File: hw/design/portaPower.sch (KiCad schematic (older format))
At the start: 5 parts

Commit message: aux output, documentation
finished aux output circuit, updated a lot of documentation, added datasheets
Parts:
- removed A?: Arduino_Nano_v3.x, Module:Arduino_Nano, symbol MCU_Module:Arduino_Nano_v3.x
- added H?: EARTH, MountingHole:MountingHole_4.3mm_M4_Pad, symbol Mechanical:MountingHole_Pad
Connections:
- net labels added: Earth_Protective, L, L_filt, N, N_filt
- wire segments 55 -> 47
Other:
- note added: "All resistors 0603 size unless otherwise stated\nAll capacitors 0603 size unless otherwise stated\nAll capacitors rated for 16V unless otherwise stated"
- note added: "Auxiliary\n5V Output"
- note added: "M4 thru hole"
- note added: "System\nRegulator"
- note removed: "Auxiliary Output &\nSecondary Regulators"
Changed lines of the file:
@@
 $Descr A4 11693 8268
 encoding utf-8
-Sheet 1 6
+Sheet 1 7
 Title ""
 Date ""
@@
 F14 "~ALT_2A" B L 5500 3550 50
 $EndSheet
-Text Notes 1350 1650 0    50   ~ 0
+Text Notes 1300 1200 0    50   ~ 0
 Line AC
 Wire Wire Line
@@
 Wire Wire Line
 	6500 3550 7600 3550
-Wire Wire Line
-	7600 3550 7600 2900
 Wire Wire Line
 	7600 1850 7950 1850
@@
 L power:GND #PWR?
 U 1 1 5EC49D4C
-P 2700 4600
-F 0 "#PWR?" H 2700 4350 50  0001 C CNN
-F 1 "GND" H 2705 4427 50  0000 C CNN
-F 2 "" H 2700 4600 50  0001 C CNN
-F 3 "" H 2700 4600 50  0001 C CNN
-	1    2700 4600
-	1    0    0    -1
-$EndComp
-Wire Wire Line
-	2700 4600 2700 4400
-Wire Wire Line
-	2700 4400 2600 4400
-Text Notes 1400 3200 0    100  ~ 0
-Auxiliary Output &\nSecondary Regulators
-$Sheet
-S 1700 3750 900  800
+P 2600 6700
+F 0 "#PWR?" H 2600 6450 50  0001 C CNN
+F 1 "GND" H 2605 6527 50  0000 C CNN
+F 2 "" H 2600 6700 50  0001 C CNN
+F 3 "" H 2600 6700 50  0001 C CNN
+	1    2600 6700
+	1    0    0    -1
+$EndComp
+Wire Wire Line
+	2600 6700 2600 6500
+Wire Wire Line
+	2600 6500 2500 6500
+Text Notes 1650 5650 0    100  ~ 0
+Auxiliary\n5V Output
+$Sheet
+S 1600 5850 900  800
 U 5EB6CA11
 F0 "AuxOut" 50
 F1 "AuxOut.sch" 50
-F2 "AuxPOut" B R 2600 3900 50
-F3 "GND" B R 2600 4400 50
-F4 "AuxIn" B L 1700 3900 50
+F2 "GND" B R 2500 6500 50
+F3 "AuxOut_I" B R 2500 6050 50
+F4 "Vbus" B L 1600 6050 50
+F5 "AuxGnd_I" B R 2500 6150 50
 $EndSheet
 Text Notes 7350 1500 0    50   ~ 0
@@
 Text Notes 2450 1800 0    50   ~ 0
 Filtered &\nProtected\nAC
-$Comp
-L MCU_Module:Arduino_Nano_v3.x A?
-U 1 1 601F5573
-P 9200 4750
-F 0 "A?" H 9550 5700 50  0000 C CNN
-F 1 "Arduino_Nano_v3.x" H 9750 3800 50  0000 C CNN
-F 2 "Module:Arduino_Nano" H 9200 4750 50  0001 C CIN
-F 3 "http://www.mouser.com/pdfdocs/Gravitech_Arduino_Nano3_0.pdf" H 9200 4750 50  0001 C CNN
-	1    9200 4750
-	1    0    0    -1
-$EndComp
-$Comp
-L power:GND #PWR?
-U 1 1 601F76A4
-P 9200 5850
-F 0 "#PWR?" H 9200 5600 50  0001 C CNN
-F 1 "GND" H 9205 5677 50  0000 C CNN
-F 2 "" H 9200 5850 50  0001 C CNN
-F 3 "" H 9200 5850 50  0001 C CNN
-	1    9200 5850
-	1    0    0    -1
-$EndComp
-Wire Wire Line
-	9200 5850 9200 5800
-Wire Wire Line
-	9200 5800 9300 5800
-Wire Wire Line
-	9300 5800 9300 5750
-Connection ~ 9200 5800
-Wire Wire Line
-	9200 5800 9200 5750
 Wire Wire Line
 	8950 1550 8950 2350
@@
 MainOut
 Wire Wire Line
-	9850 2900 7600 2900
-Connection ~ 7600 2900
-Wire Wire Line
-	7600 2900 7600 1850
-Wire Wire Line
-	9700 5150 10250 5150
-Wire Wire Line
-	9700 5250 10250 5250
-Text Label 10250 5150 2    50   ~ 0
-SDA
-Text Label 10250 5250 2    50   ~ 0
-SCL
-Wire Wire Line
 	5000 3950 5500 3950
 Wire Wire Line
@@
 Text Label 5000 4050 0    50   ~ 0
 SCL
-Wire Wire Line
-	10600 4850 9700 4850
-Wire Wire Line
-	10600 2800 10600 4850
-Wire Wire Line
-	9850 2900 9850 4950
-Wire Wire Line
-	9850 4950 9700 4950
+Text Notes 1700 4100 0    100  ~ 0
+System\nRegulator
+Text Label 1550 1500 2    50   ~ 0
+L
+Text Label 1450 1700 2    50   ~ 0
+N
+Wire Wire Line
+	1250 1900 1400 1900
+Wire Wire Line
+	1400 1900 1400 2300
+$Comp
+L power:Earth_Protective #PWR?
+U 1 1 60430B87
+P 1400 2350
+F 0 "#PWR?" H 1650 2100 50  0001 C CNN
+F 1 "Earth_Protective" H 1850 2200 50  0001 C CNN
+F 2 "" H 1400 2250 50  0001 C CNN
+F 3 "~" H 1400 2250 50  0001 C CNN
+	1    1400 2350
+	1    0    0    -1
+$EndComp
+$Comp
+L Mechanical:MountingHole_Pad H?
+U 1 1 6043152A
+P 1200 2300
+F 0 "H?" V 1250 2650 50  0000 C CNN
+F 1 "EARTH" V 1150 2600 50  0000 C CNN
+F 2 "MountingHole:MountingHole_4.3mm_M4_Pad" H 1200 2300 50  0001 C CNN
+F 3 "~" H 1200 2300 50  0001 C CNN
+	1    1200 2300
+	0    -1   -1   0
+$EndComp
+Wire Wire Line
+	1300 2300 1400 2300
+Connection ~ 1400 2300
+Wire Wire Line
+	1400 2300 1400 2350
+Text Notes 700  2550 0    50   ~ 0
+M4 thru hole
+Text Label 2500 1500 0    50   ~ 0
+L_filt
+Text Label 2500 1850 0    50   ~ 0
+N_filt
+Wire Wire Line
+	7600 1850 7600 3550
+$Sheet
+S 1600 4250 900  850
+U 604399F3
+F0 "SysPower" 50
+F1 "SysPower.sch" 50
+F2 "Vbus" I L 1600 4400 50
+F3 "GND" B R 2500 5000 50
+F4 "PGOOD" O L 1600 4750 50
+F5 "5V" O R 2500 4400 50
+$EndSheet
+Text Notes 900  7500 0    50   ~ 0
+All resistors 0603 size unless otherwise stated\nAll capacitors 0603 size unless otherwise stated\nAll capacitors rated for 16V unless otherwise stated
 $EndSCHEMATC

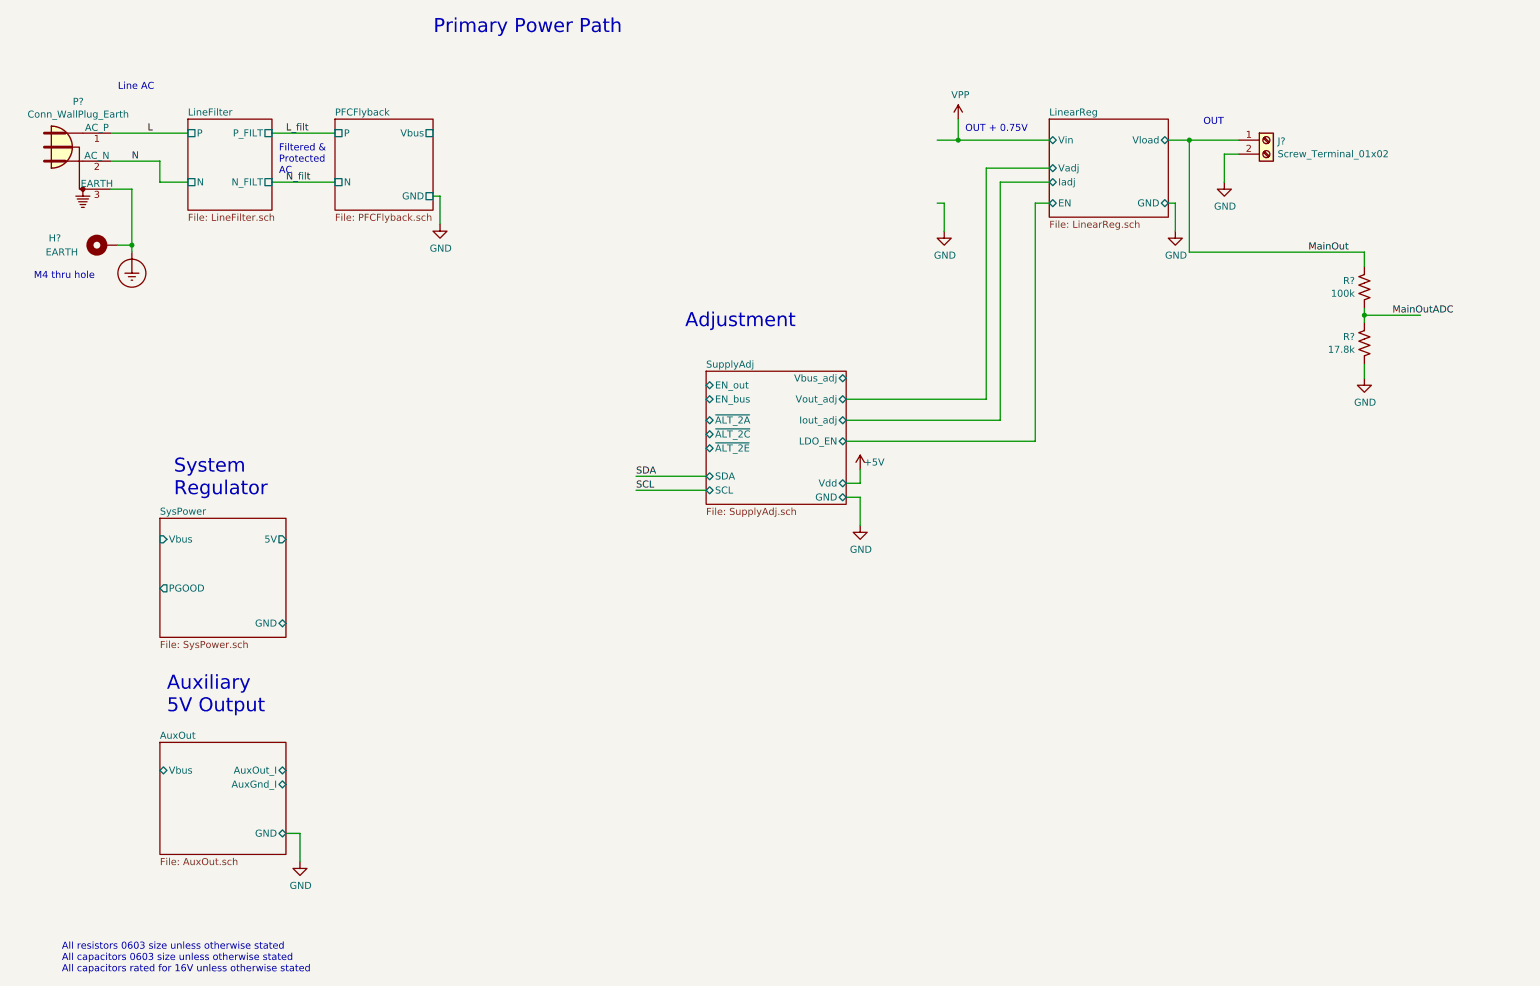
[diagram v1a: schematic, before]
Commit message: reworked adjusters
new V/I adjustment scheme; modified LDO circuit to match
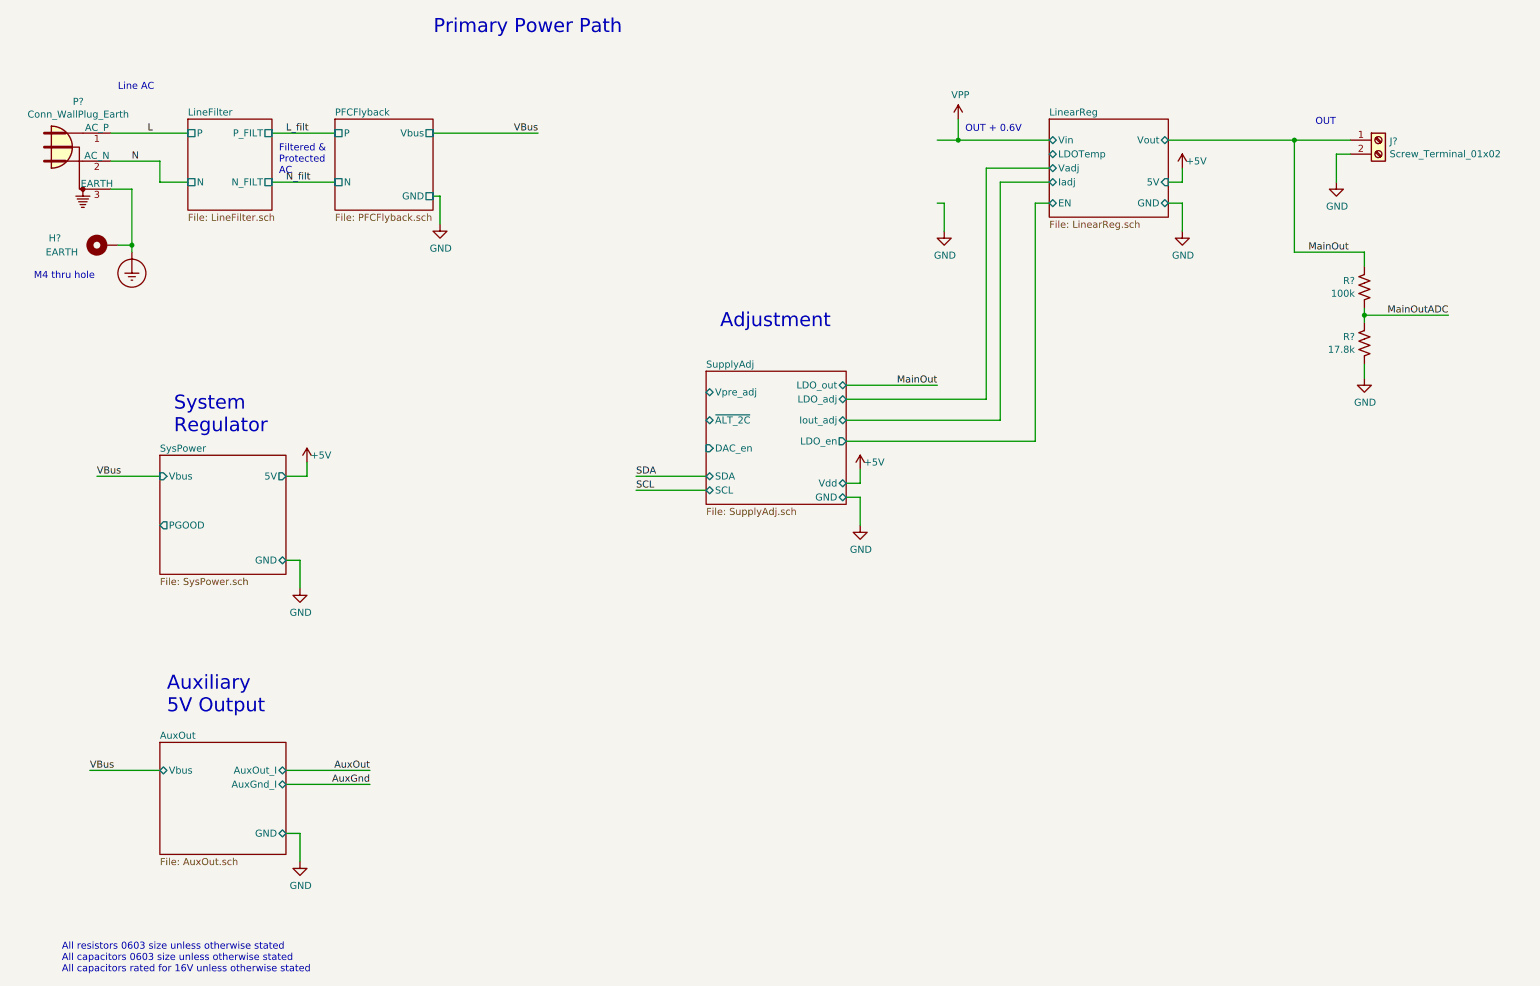
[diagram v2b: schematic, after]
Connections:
- net labels added: AuxGnd, AuxOut, VBus
- wire segments 47 -> 59
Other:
- note added: "OUT + 0.6V"
- note removed: "OUT + 0.75V"
- moved on the sheet: J?
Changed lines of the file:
@@
 L power:GND #PWR?
 U 1 1 5E888D15
-P 8850 2200
-F 0 "#PWR?" H 8850 1950 50  0001 C CNN
-F 1 "GND" H 8855 2027 50  0000 C CNN
-F 2 "" H 8850 2200 50  0001 C CNN
-F 3 "" H 8850 2200 50  0001 C CNN
-	1    8850 2200
-	1    0    0    -1
-$EndComp
-Wire Wire Line
-	8850 2200 8850 2000
+P 8900 2200
+F 0 "#PWR?" H 8900 1950 50  0001 C CNN
+F 1 "GND" H 8905 2027 50  0000 C CNN
+F 2 "" H 8900 2200 50  0001 C CNN
+F 3 "" H 8900 2200 50  0001 C CNN
+	1    8900 2200
+	1    0    0    -1
+$EndComp
+Wire Wire Line
+	8900 2200 8900 2000
 Wire Wire Line
 	7200 2000 7150 2000
@@
 F2 "GND" B R 8800 2000 50
 F3 "Vin" B L 7950 1550 50
-F4 "Vload" B R 8800 1550 50
-F5 "Vadj" B L 7950 1750 50
-F6 "Iadj" B L 7950 1850 50
-F7 "EN" B L 7950 2000 50
-$EndSheet
-Wire Wire Line
-	8850 2000 8800 2000
+F4 "Iadj" B L 7950 1850 50
+F5 "EN" B L 7950 2000 50
+F6 "Vout" B R 8800 1550 50
+F7 "LDOTemp" B L 7950 1650 50
+F8 "Vadj" B L 7950 1750 50
+F9 "5V" I R 8800 1850 50
+$EndSheet
+Wire Wire Line
+	8900 2000 8800 2000
 Connection ~ 7300 1550
 Wire Wire Line
@@
 F1 "SupplyAdj.sch" 50
 F2 "GND" B R 6500 4100 50
-F3 "Vout_adj" B R 6500 3400 50
-F4 "Iout_adj" B R 6500 3550 50
-F5 "EN_out" B L 5500 3300 50
-F6 "SCL" B L 5500 4050 50
-F7 "SDA" B L 5500 3950 50
-F8 "Vdd" B R 6500 4000 50
-F9 "~ALT_2C" B L 5500 3650 50
-F10 "~ALT_2E" B L 5500 3750 50
-F11 "LDO_EN" B R 6500 3700 50
-F12 "Vbus_adj" B R 6500 3250 50
-F13 "EN_bus" B L 5500 3400 50
-F14 "~ALT_2A" B L 5500 3550 50
+F3 "Iout_adj" B R 6500 3550 50
+F4 "SCL" B L 5500 4050 50
+F5 "SDA" B L 5500 3950 50
+F6 "Vdd" B R 6500 4000 50
+F7 "~ALT_2C" B L 5500 3550 50
+F8 "LDO_out" B R 6500 3300 50
+F9 "Vpre_adj" B L 5500 3350 50
+F10 "LDO_adj" B R 6500 3400 50
+F11 "LDO_en" O R 6500 3700 50
+F12 "DAC_en" I L 5500 3750 50
 $EndSheet
 Text Notes 1300 1200 0    50   ~ 0
@@
 Wire Wire Line
 	6600 3900 6600 4000
-Text Notes 5350 2900 0    100  ~ 0
+Text Notes 5600 2900 0    100  ~ 0
 Adjustment
 $Comp
@@
 $EndSheet
 Text Notes 7350 1500 0    50   ~ 0
-OUT + 0.75V
+OUT + 0.6V
 $Comp
 L Connector:Screw_Terminal_01x02 J?
 U 1 1 5ECE72C5
-P 9500 1550
-F 0 "J?" H 9580 1542 50  0000 L CNN
-F 1 "Screw_Terminal_01x02" H 9580 1451 50  0000 L CNN
-F 2 "" H 9500 1550 50  0001 C CNN
-F 3 "~" H 9500 1550 50  0001 C CNN
-	1    9500 1550
-	1    0    0    -1
-$EndComp
-Wire Wire Line
-	9300 1550 8950 1550
+P 10300 1550
+F 0 "J?" H 10380 1542 50  0000 L CNN
+F 1 "Screw_Terminal_01x02" H 10380 1451 50  0000 L CNN
+F 2 "" H 10300 1550 50  0001 C CNN
+F 3 "~" H 10300 1550 50  0001 C CNN
+	1    10300 1550
+	1    0    0    -1
+$EndComp
+Wire Wire Line
+	10100 1550 9700 1550
 $Comp
 L power:GND #PWR?
 U 1 1 5ECE7CAE
-P 9200 1850
-F 0 "#PWR?" H 9200 1600 50  0001 C CNN
-F 1 "GND" H 9205 1677 50  0000 C CNN
-F 2 "" H 9200 1850 50  0001 C CNN
-F 3 "" H 9200 1850 50  0001 C CNN
-	1    9200 1850
-	1    0    0    -1
-$EndComp
-Wire Wire Line
-	9200 1850 9200 1650
-Wire Wire Line
-	9200 1650 9300 1650
-Text Notes 9050 1450 0    50   ~ 0
+P 10000 1850
+F 0 "#PWR?" H 10000 1600 50  0001 C CNN
+F 1 "GND" H 10005 1677 50  0000 C CNN
+F 2 "" H 10000 1850 50  0001 C CNN
+F 3 "" H 10000 1850 50  0001 C CNN
+	1    10000 1850
+	1    0    0    -1
+$EndComp
+Wire Wire Line
+	10000 1850 10000 1650
+Wire Wire Line
+	10000 1650 10100 1650
+Text Notes 9850 1450 0    50   ~ 0
 OUT
 Wire Wire Line
@@
 Filtered &\nProtected\nAC
 Wire Wire Line
-	8950 1550 8950 2350
-Connection ~ 8950 1550
-Wire Wire Line
-	8950 1550 8800 1550
+	9700 1550 9700 2350
+Connection ~ 9700 1550
+Wire Wire Line
+	9700 1550 8800 1550
 $Comp
 L Device:R_US R?
@@
 	10200 2350 10200 2450
 Wire Wire Line
-	8950 2350 10200 2350
+	9700 2350 10200 2350
 Wire Wire Line
 	10200 2750 10200 2800
@@
 	10200 3250 10200 3150
 Wire Wire Line
-	10200 2800 10600 2800
+	10200 2800 10800 2800
 Connection ~ 10200 2800
 Wire Wire Line
 	10200 2800 10200 2850
-Text Label 10400 2800 0    50   ~ 0
+Text Label 10800 2800 2    50   ~ 0
 MainOutADC
 Text Label 9800 2350 0    50   ~ 0
@@
 Text Label 5000 4050 0    50   ~ 0
 SCL
-Text Notes 1700 4100 0    100  ~ 0
+Text Notes 1700 3650 0    100  ~ 0
 System\nRegulator
 Text Label 1550 1500 2    50   ~ 0
@@
 	7600 1850 7600 3550
 $Sheet
-S 1600 4250 900  850
+S 1600 3800 900  850
 U 604399F3
 F0 "SysPower" 50
 F1 "SysPower.sch" 50
-F2 "Vbus" I L 1600 4400 50
-F3 "GND" B R 2500 5000 50
-F4 "PGOOD" O L 1600 4750 50
-F5 "5V" O R 2500 4400 50
+F2 "Vbus" I L 1600 3950 50
+F3 "GND" B R 2500 4550 50
+F4 "PGOOD" O L 1600 4300 50
+F5 "5V" O R 2500 3950 50
 $EndSheet
 Text Notes 900  7500 0    50   ~ 0
 All resistors 0603 size unless otherwise stated\nAll capacitors 0603 size unless otherwise stated\nAll capacitors rated for 16V unless otherwise stated
+Wire Wire Line
+	6500 3300 7150 3300
+Text Label 7150 3300 2    50   ~ 0
+MainOut
+Wire Wire Line
+	2500 6050 3100 6050
+Text Label 3100 6050 2    50   ~ 0
+AuxOut
+Wire Wire Line
+	2500 6150 3100 6150
+Text Label 3100 6150 2    50   ~ 0
+AuxGnd
+Wire Wire Line
+	3550 1500 4300 1500
+Text Label 4300 1500 2    50   ~ 0
+VBus
+Wire Wire Line
+	1150 3950 1600 3950
+Text Label 1150 3950 0    50   ~ 0
+VBus
+Text Label 1100 6050 0    50   ~ 0
+VBus
+Wire Wire Line
+	1100 6050 1600 6050
+$Comp
+L power:+5V #PWR?
+U 1 1 6035C946
+P 2650 3850
+F 0 "#PWR?" H 2650 3700 50  0001 C CNN
+F 1 "+5V" H 2750 3900 50  0000 C CNN
+F 2 "" H 2650 3850 50  0001 C CNN
+F 3 "" H 2650 3850 50  0001 C CNN
+	1    2650 3850
+	1    0    0    -1
+$EndComp
+Wire Wire Line
+	2650 3850 2650 3950
+Wire Wire Line
+	2650 3950 2500 3950
+$Comp
+L power:GND #PWR?
+U 1 1 6035E40E
+P 2600 4750
+F 0 "#PWR?" H 2600 4500 50  0001 C CNN
+F 1 "GND" H 2605 4577 50  0000 C CNN
+F 2 "" H 2600 4750 50  0001 C CNN
+F 3 "" H 2600 4750 50  0001 C CNN
+	1    2600 4750
+	1    0    0    -1
+$EndComp
+Wire Wire Line
+	2600 4750 2600 4550
+Wire Wire Line
+	2600 4550 2500 4550
+$Comp
+L power:+5V #PWR?
+U 1 1 603ACEF5
+P 8900 1750
+F 0 "#PWR?" H 8900 1600 50  0001 C CNN
+F 1 "+5V" H 9000 1800 50  0000 C CNN
+F 2 "" H 8900 1750 50  0001 C CNN
+F 3 "" H 8900 1750 50  0001 C CNN
+	1    8900 1750
+	1    0    0    -1
+$EndComp
+Wire Wire Line
+	8900 1750 8900 1850
+Wire Wire Line
+	8900 1850 8800 1850
 $EndSCHEMATC

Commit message: label/net reorg, primary SW starting
some reorganization of top-level naming for nets and hierarchical pins

fixed a few part selection issues

started on primary switcher sheet
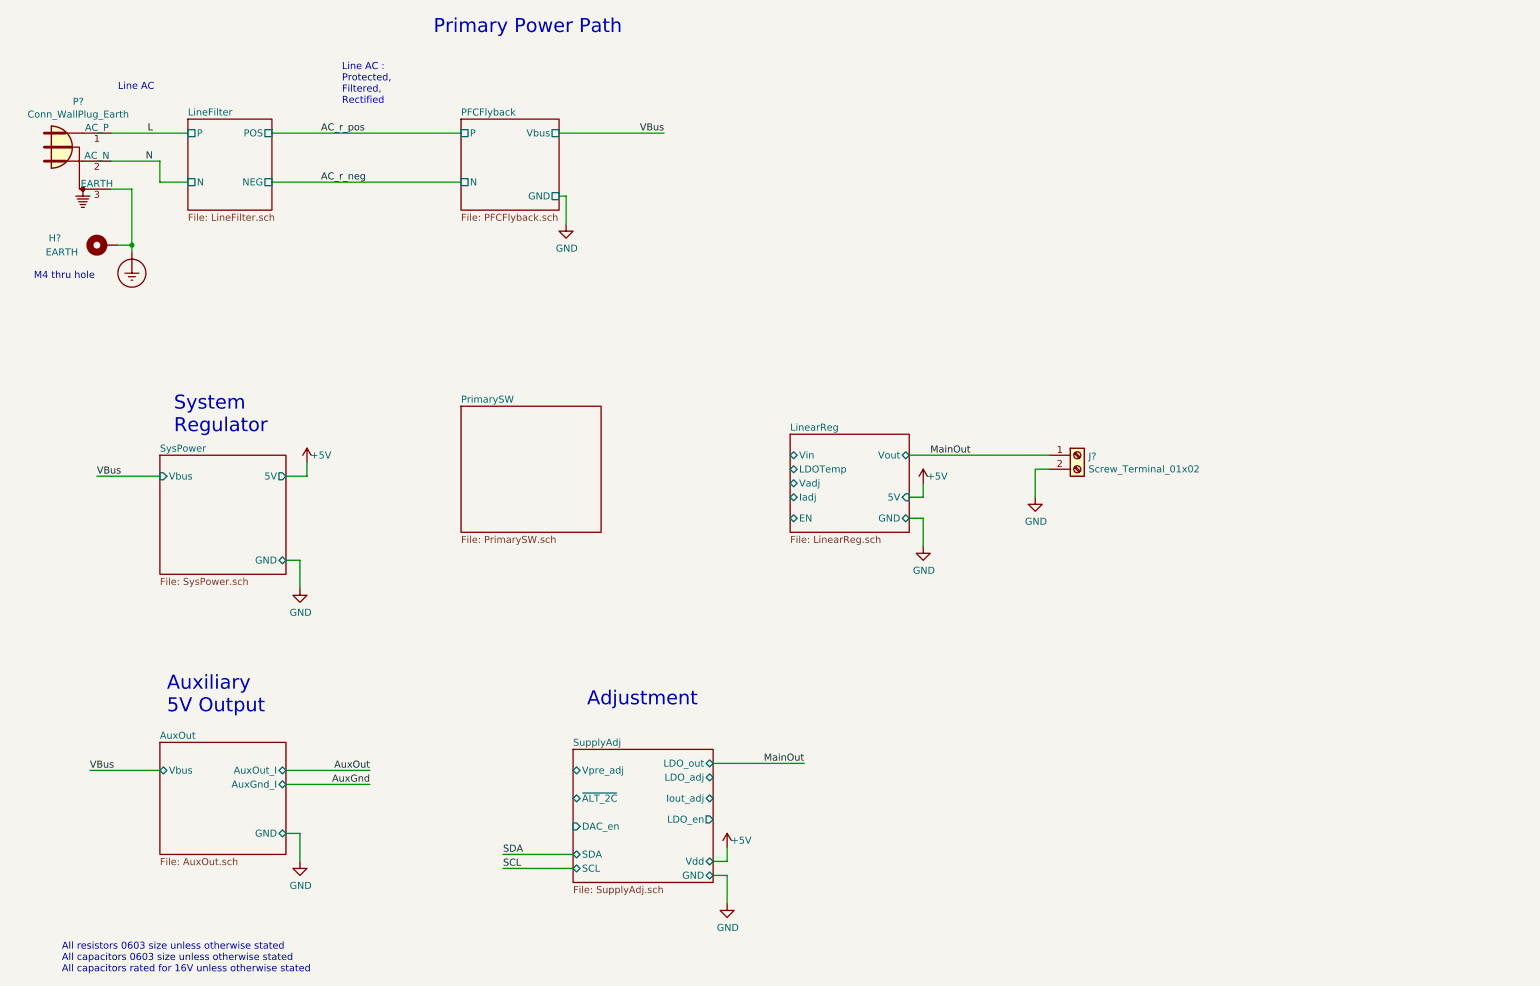
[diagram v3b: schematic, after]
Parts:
- removed R?: 100k, Resistor_SMD:R_0603_1608Metric, symbol Device:R_US
- removed R?: 17.8k, Resistor_SMD:R_0603_1608Metric, symbol Device:R_US
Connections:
- net labels added: AC_r_neg, AC_r_pos
- net labels removed: L_filt, MainOutADC, N_filt, VPP
- wire segments 59 -> 37
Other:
- note added: "Line AC :\nProtected,\nFiltered,\nRectified"
- note removed: "Filtered &\nProtected\nAC"
- note removed: "OUT"
- note removed: "OUT + 0.6V"
- moved on the sheet: J?
